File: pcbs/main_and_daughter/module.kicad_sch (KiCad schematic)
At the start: 3 parts

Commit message: added titles to schematic
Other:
- title: (none) -> Module Bay
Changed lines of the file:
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@@
 	(generator_version "10.0")
 	(paper "A5")
+	(title_block
+		(title "Module Bay")
+	)
 	(text "E24 for the module detect resistors\n1k->10k, 10k->100k\n0.1%"
 		(exclude_from_sim no)

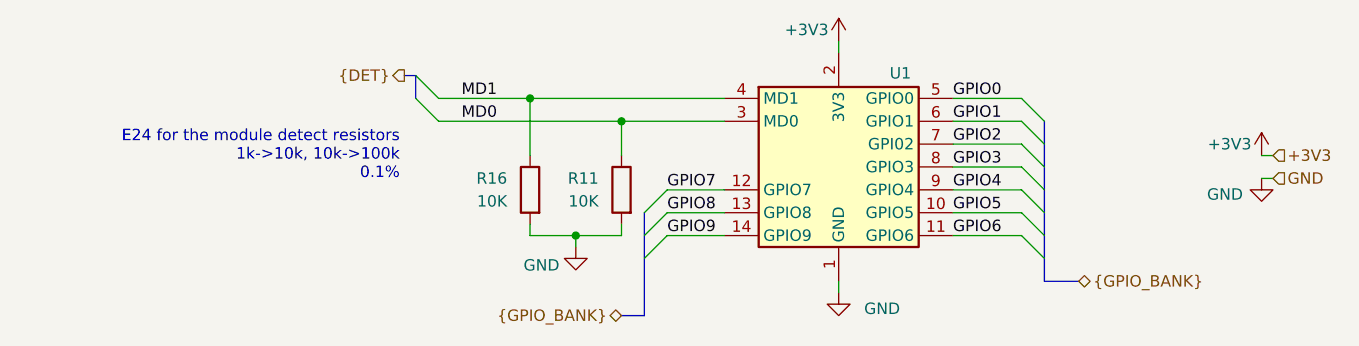
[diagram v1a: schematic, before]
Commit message: added lcsc part nums
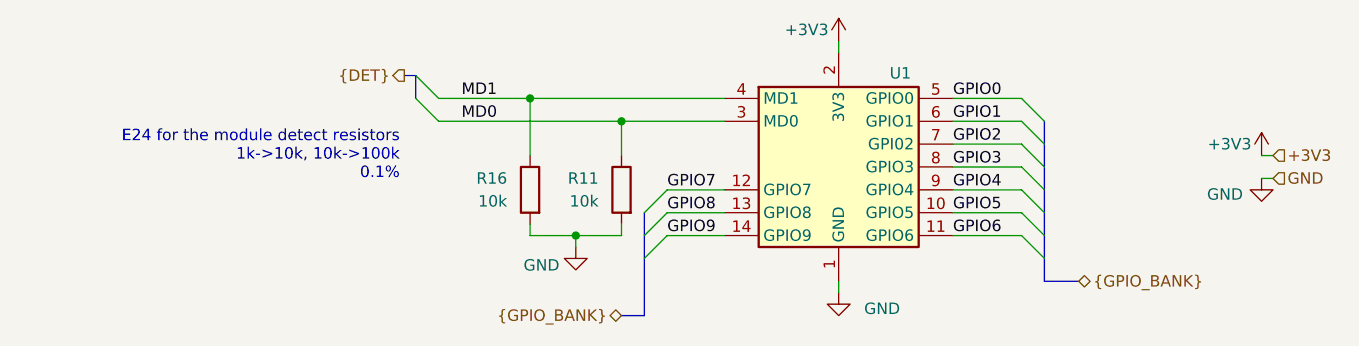
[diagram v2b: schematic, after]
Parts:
- R11, R16: value 10K -> 10k; LCSC (none) -> C2906861
- U1: now left out of the parts list
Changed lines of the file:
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@@
 			)
 		)
-		(property "Value" "10K"
+		(property "Value" "10k"
 			(at 78.74 64.7699 0)
 			(show_name no)
@@
 		)
 		(property "Description" "Resistor"
+			(at 81.28 63.5 0)
+			(hide yes)
+			(show_name no)
+			(do_not_autoplace no)
+			(effects
+				(font
+					(size 1.27 1.27)
+				)
+			)
+		)
+		(property "LCSC" "C2906861"
 			(at 81.28 63.5 0)
 			(hide yes)
@@
 			)
 		)
-		(property "Value" "10K"
+		(property "Value" "10k"
 			(at 68.58 64.7699 0)
 			(show_name no)
@@
 		)
 		(property "Description" "Resistor"
+			(at 71.12 63.5 0)
+			(hide yes)
+			(show_name no)
+			(do_not_autoplace no)
+			(effects
+				(font
+					(size 1.27 1.27)
+				)
+			)
+		)
+		(property "LCSC" "C2906861"
 			(at 71.12 63.5 0)
 			(hide yes)
@@
 		(body_style 1)
 		(exclude_from_sim no)
-		(in_bom yes)
+		(in_bom no)
 		(on_board yes)
 		(in_pos_files yes)
